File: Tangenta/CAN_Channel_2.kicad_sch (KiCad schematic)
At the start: 18 parts, among them J22 Conn_01x02_Pin, Q3 BSS138, U20 ADM3053

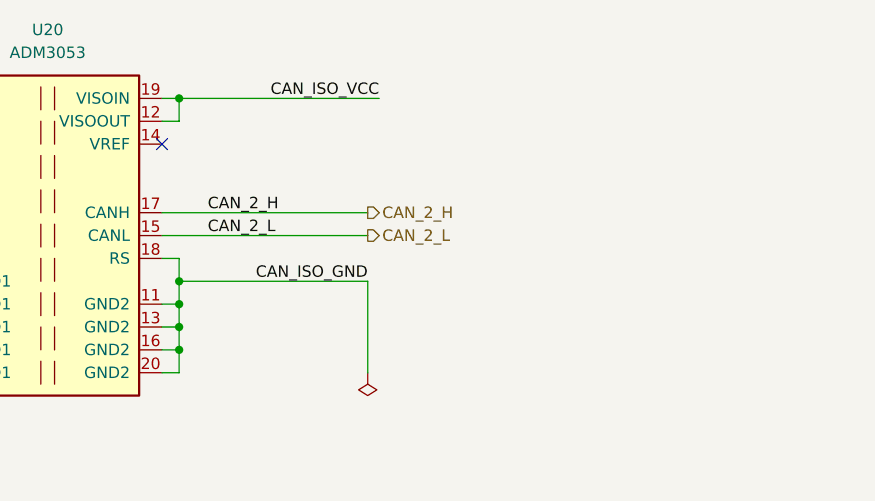
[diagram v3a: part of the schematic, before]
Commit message: CANbus done, UART terminals in progress...
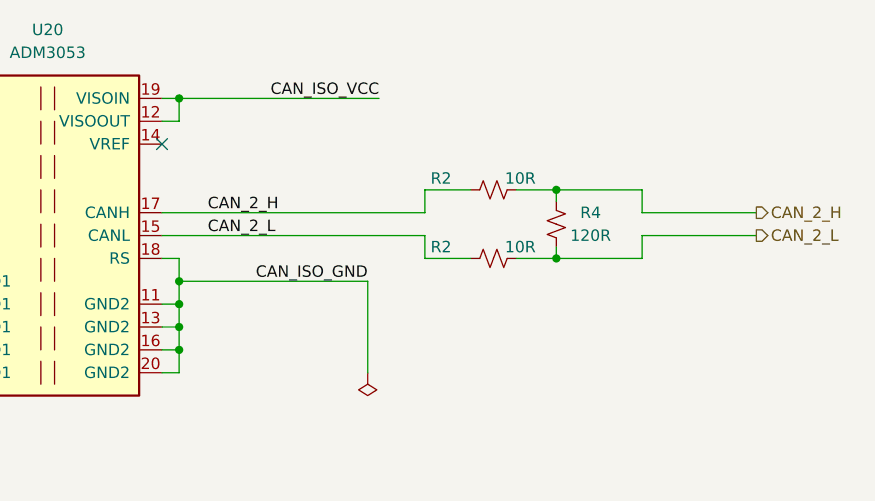
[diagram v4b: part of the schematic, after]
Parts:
- added R2 (x2): 10R, Resistor_SMD:R_0402_1005Metric, symbol Device:R_Small_US
- added R4: 120R, Resistor_SMD:R_0603_1608Metric, symbol Device:R_Small_US
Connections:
- net CAN_2_H: now also R2.1, R2.2, R4.1
- net CAN_2_L: now also R2.1, R2.2, R4.2
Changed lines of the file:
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@@
   (junction (at 124.46 140.97) (diameter 0) (color 0 0 0 0)
   )
+  (junction (at 193.675 77.47) (diameter 0) (color 0 0 0 0)
+  )
   (junction (at 124.46 130.81) (diameter 0) (color 0 0 0 0)
   )
@@
   (junction (at 122.555 85.09) (diameter 0) (color 0 0 0 0)
   )
+  (junction (at 193.675 69.85) (diameter 0) (color 0 0 0 0)
+  )
   (junction (at 80.01 140.97) (diameter 0) (color 0 0 0 0)
   )
@@
   )
   (no_connect (at 149.86 64.77))
+  (wire (pts (xy 193.675 69.85) (xy 193.675 71.12))
+    (stroke (width 0) (type default))
+  )
   (wire (pts (xy 124.46 119.38) (xy 124.46 121.92))
     (stroke (width 0) (type default))
@@
     (stroke (width 0) (type default))
   )
-  (wire (pts (xy 149.86 72.39) (xy 172.72 72.39))
+  (wire (pts (xy 149.86 72.39) (xy 179.07 72.39))
     (stroke (width 0) (type default))
   )
@@
     (stroke (width 0) (type default))
   )
+  (wire (pts (xy 215.9 74.93) (xy 203.2 74.93))
+    (stroke (width 0) (type default))
+  )
   (wire (pts (xy 151.765 90.17) (xy 151.765 87.63))
     (stroke (width 0) (type default))
@@
     (stroke (width 0) (type default))
   )
+  (wire (pts (xy 203.2 69.85) (xy 193.675 69.85))
+    (stroke (width 0) (type default))
+  )
   (wire (pts (xy 151.765 59.69) (xy 173.99 59.69))
     (stroke (width 0) (type default))
@@
     (stroke (width 0) (type default))
   )
+  (wire (pts (xy 189.23 69.85) (xy 193.675 69.85))
+    (stroke (width 0) (type default))
+  )
   (wire (pts (xy 141.605 111.76) (xy 141.605 114.3))
     (stroke (width 0) (type default))
@@
     (stroke (width 0) (type default))
   )
+  (wire (pts (xy 179.07 74.93) (xy 179.07 77.47))
+    (stroke (width 0) (type default))
+  )
   (wire (pts (xy 29.21 140.97) (xy 53.34 140.97))
     (stroke (width 0) (type default))
@@
     (stroke (width 0) (type default))
   )
+  (wire (pts (xy 179.07 72.39) (xy 179.07 69.85))
+    (stroke (width 0) (type default))
+  )
   (wire (pts (xy 122.555 59.69) (xy 113.03 59.69))
     (stroke (width 0) (type default))
   )
+  (wire (pts (xy 189.23 77.47) (xy 193.675 77.47))
+    (stroke (width 0) (type default))
+  )
   (wire (pts (xy 113.03 130.81) (xy 124.46 130.81))
     (stroke (width 0) (type default))
@@
     (stroke (width 0) (type default))
   )
+  (wire (pts (xy 179.07 77.47) (xy 184.15 77.47))
+    (stroke (width 0) (type default))
+  )
   (wire (pts (xy 172.085 140.97) (xy 178.435 140.97))
     (stroke (width 0) (type default))
@@
     (stroke (width 0) (type default))
   )
+  (wire (pts (xy 179.07 69.85) (xy 184.15 69.85))
+    (stroke (width 0) (type default))
+  )
   (wire (pts (xy 53.34 128.27) (xy 53.34 132.08))
     (stroke (width 0) (type default))
@@
     (stroke (width 0) (type default))
   )
-  (wire (pts (xy 149.86 74.93) (xy 172.72 74.93))
+  (wire (pts (xy 149.86 74.93) (xy 179.07 74.93))
     (stroke (width 0) (type default))
   )
@@
     (stroke (width 0) (type default))
   )
+  (wire (pts (xy 193.675 76.2) (xy 193.675 77.47))
+    (stroke (width 0) (type default))
+  )
   (wire (pts (xy 124.46 64.77) (xy 122.555 64.77))
     (stroke (width 0) (type default))
@@
     (stroke (width 0) (type default))
   )
+  (wire (pts (xy 203.2 72.39) (xy 203.2 69.85))
+    (stroke (width 0) (type default))
+  )
   (wire (pts (xy 172.72 90.17) (xy 172.72 80.01))
     (stroke (width 0) (type default))
   )
+  (wire (pts (xy 215.9 72.39) (xy 203.2 72.39))
+    (stroke (width 0) (type default))
+  )
   (wire (pts (xy 151.765 77.47) (xy 149.86 77.47))
     (stroke (width 0) (type default))
@@
   )
   (wire (pts (xy 132.08 119.38) (xy 132.08 121.92))
+    (stroke (width 0) (type default))
+  )
+  (wire (pts (xy 203.2 77.47) (xy 193.675 77.47))
+    (stroke (width 0) (type default))
+  )
+  (wire (pts (xy 203.2 74.93) (xy 203.2 77.47))
     (stroke (width 0) (type default))
   )
@@
     (effects (font (size 1.27 1.27)) (justify right))
   )
-  (hierarchical_label "CAN_2_L" (shape output) (at 172.72 74.93 0) (fields_autoplaced)
+  (hierarchical_label "CAN_2_L" (shape output) (at 215.9 74.93 0) (fields_autoplaced)
     (effects (font (size 1.27 1.27)) (justify left))
   )
-  (hierarchical_label "CAN_2_H" (shape output) (at 172.72 72.39 0) (fields_autoplaced)
+  (hierarchical_label "CAN_2_H" (shape output) (at 215.9 72.39 0) (fields_autoplaced)
     (effects (font (size 1.27 1.27)) (justify left))
   )
@@
     )
   )
+  (symbol (lib_id "Device:R_Small_US") (at 193.675 73.66 0) (unit 1)
+    (in_bom yes) (on_board yes) (dnp no)
+    (property "Reference" "R4" (at 197.485 72.39 0)
+      (effects (font (size 1.27 1.27)))
+    )
+    (property "Value" "120R" (at 197.485 74.93 0)
+      (effects (font (size 1.27 1.27)))
+    )
+    (property "Footprint" "Resistor_SMD:R_0603_1608Metric" (at 193.675 73.66 0)
+      (effects (font (size 1.27 1.27)) hide)
+    )
+    (property "Datasheet" "~" (at 193.675 73.66 0)
+      (effects (font (size 1.27 1.27)) hide)
+    )
+    (pin "1")
+    (pin "2")
+    (instances
+      (project "Tangenta"
+        (path "/358d1bcf-7599-4352-8c4d-baa18a5f09e6/8215796b-9611-4f43-bcc5-319f8414b8a6"
+          (reference "R4") (unit 1)
+        )
+        (path "/358d1bcf-7599-4352-8c4d-baa18a5f09e6/98e3b24f-9927-4339-b8fd-9deea91a522a"
+          (reference "R182") (unit 1)
+        )
+        (path "/358d1bcf-7599-4352-8c4d-baa18a5f09e6/b5394a48-5ef8-44c9-9d56-604d4ce6d7c8/96e01dc6-7803-4642-812e-1845a7add5da"
+          (reference "R184") (unit 1)
+        )
+        (path "/358d1bcf-7599-4352-8c4d-baa18a5f09e6/b5394a48-5ef8-44c9-9d56-604d4ce6d7c8/9d7e074a-447f-4471-b1b0-91eb27649d54"
+          (reference "R187") (unit 1)
+        )
+      )
+    )
+  )
   (symbol (lib_id "power:GNDREF") (at 113.03 140.97 0) (unit 1)
     (in_bom yes) (on_board yes) (dnp no) (fields_autoplaced)
@@
         )
       )
+    )
+  )
+  (symbol (lib_id "Device:R_Small_US") (at 186.69 77.47 270) (unit 1)
+    (in_bom yes) (on_board yes) (dnp no)
+    (property "Reference" "R2" (at 179.705 76.2 90)
+      (effects (font (size 1.27 1.27)) (justify left))
+    )
+    (property "Value" "10R" (at 187.96 76.2 90)
+      (effects (font (size 1.27 1.27)) (justify left))
+    )
+    (property "Footprint" "Resistor_SMD:R_0402_1005Metric" (at 186.69 77.47 0)
+      (effects (font (size 1.27 1.27)) hide)
+    )
+    (property "Datasheet" "~" (at 186.69 77.47 0)
+      (effects (font (size 1.27 1.27)) hide)
+    )
+    (pin "1")
+    (pin "2")
+    (instances
+      (project "Tangenta"
+        (path "/358d1bcf-7599-4352-8c4d-baa18a5f09e6/8215796b-9611-4f43-bcc5-319f8414b8a6"
+          (reference "R2") (unit 1)
+        )
+        (path "/358d1bcf-7599-4352-8c4d-baa18a5f09e6/d6c05402-162e-441f-bed8-be7996260fb4"
+          (reference "R18") (unit 1)
+        )
+        (path "/358d1bcf-7599-4352-8c4d-baa18a5f09e6/b1871a4d-6a35-44e2-a9a2-9a4af684371d"
+          (reference "R26") (unit 1)
+        )
+        (path "/358d1bcf-7599-4352-8c4d-baa18a5f09e6/6a8c68b5-4a7d-449e-86f6-34ced6d1cb55"
+          (reference "R41") (unit 1)
+        )
+        (path "/358d1bcf-7599-4352-8c4d-baa18a5f09e6/db297b0b-35f2-4e86-892c-83973f1ac2db"
+          (reference "R41") (unit 1)
+        )
+        (path "/358d1bcf-7599-4352-8c4d-baa18a5f09e6/98e3b24f-9927-4339-b8fd-9deea91a522a"
+          (reference "R153") (unit 1)
+        )
+        (path "/358d1bcf-7599-4352-8c4d-baa18a5f09e6/b5394a48-5ef8-44c9-9d56-604d4ce6d7c8/96e01dc6-7803-4642-812e-1845a7add5da"
+          (reference "R168") (unit 1)
+        )
+        (path "/358d1bcf-7599-4352-8c4d-baa18a5f09e6/b5394a48-5ef8-44c9-9d56-604d4ce6d7c8/9d7e074a-447f-4471-b1b0-91eb27649d54"
+          (reference "R186") (unit 1)
+        )
+      )
+    )
+  )
+  (symbol (lib_id "Device:R_Small_US") (at 186.69 69.85 270) (unit 1)
+    (in_bom yes) (on_board yes) (dnp no)
+    (property "Reference" "R2" (at 179.705 68.58 90)
+      (effects (font (size 1.27 1.27)) (justify left))
+    )
+    (property "Value" "10R" (at 187.96 68.58 90)
+      (effects (font (size 1.27 1.27)) (justify left))
+    )
+    (property "Footprint" "Resistor_SMD:R_0402_1005Metric" (at 186.69 69.85 0)
+      (effects (font (size 1.27 1.27)) hide)
+    )
+    (property "Datasheet" "~" (at 186.69 69.85 0)
+      (effects (font (size 1.27 1.27)) hide)
+    )
+    (pin "1")
+    (pin "2")
+    (instances
+      (project "Tangenta"
+        (path "/358d1bcf-7599-4352-8c4d-baa18a5f09e6/8215796b-9611-4f43-bcc5-319f8414b8a6"
+          (reference "R2") (unit 1)
+        )
+        (path "/358d1bcf-7599-4352-8c4d-baa18a5f09e6/d6c05402-162e-441f-bed8-be7996260fb4"
+          (reference "R18") (unit 1)
+        )
+        (path "/358d1bcf-7599-4352-8c4d-baa18a5f09e6/b1871a4d-6a35-44e2-a9a2-9a4af684371d"
+          (reference "R26") (unit 1)
+        )
+        (path "/358d1bcf-7599-4352-8c4d-baa18a5f09e6/6a8c68b5-4a7d-449e-86f6-34ced6d1cb55"
+          (reference "R41") (unit 1)
+        )
+        (path "/358d1bcf-7599-4352-8c4d-baa18a5f09e6/db297b0b-35f2-4e86-892c-83973f1ac2db"
+          (reference "R41") (unit 1)
+        )
+        (path "/358d1bcf-7599-4352-8c4d-baa18a5f09e6/98e3b24f-9927-4339-b8fd-9deea91a522a"
+          (reference "R152") (unit 1)
+        )
+        (path "/358d1bcf-7599-4352-8c4d-baa18a5f09e6/b5394a48-5ef8-44c9-9d56-604d4ce6d7c8/96e01dc6-7803-4642-812e-1845a7add5da"
+          (reference "R151") (unit 1)
+        )
+        (path "/358d1bcf-7599-4352-8c4d-baa18a5f09e6/b5394a48-5ef8-44c9-9d56-604d4ce6d7c8/9d7e074a-447f-4471-b1b0-91eb27649d54"
+          (reference "R185") (unit 1)
+        )
+      )

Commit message: Libraries exported from global to project.
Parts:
- C1: symbol Device:C_Small -> CholaSymbolsPrjLib:C_Small
- FB1: symbol Ferrite_Bead_100:GZ2012D101TF -> CholaSymbolsPrjLib:GZ2012D101TF
- J22: symbol Connector:Conn_01x02_Pin -> CholaSymbolsPrjLib:Conn_01x02_Pin
- Q3: symbol Transistor_FET:BSS138 -> CholaSymbolsPrjLib:BSS138
- R2, R4: symbol Device:R_Small_US -> CholaSymbolsPrjLib:R_Small_US
- U20: symbol Interface_CAN_LIN:ADM3053 -> CholaSymbolsPrjLib:ADM3053
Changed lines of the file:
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@@
     (effects (font (size 1.27 1.27)) (justify left))
   )
-  (symbol (lib_id "Device:R_Small_US") (at 80.01 134.62 180) (unit 1)
+  (symbol (lib_id "CholaSymbolsPrjLib:R_Small_US") (at 80.01 134.62 180) (unit 1)
     (in_bom yes) (on_board yes) (dnp no)
     (property "Reference" "R2" (at 78.74 133.35 0)
@@
     )
   )
-  (symbol (lib_id "Transistor_FET:BSS138") (at 66.04 138.43 270) (unit 1)
+  (symbol (lib_id "CholaSymbolsPrjLib:BSS138") (at 66.04 138.43 270) (unit 1)
     (in_bom yes) (on_board yes) (dnp no)
     (property "Reference" "Q3" (at 68.58 135.89 90)
@@
     )
   )
-  (symbol (lib_id "Device:C_Small") (at 132.08 135.89 180) (unit 1)
+  (symbol (lib_id "CholaSymbolsPrjLib:C_Small") (at 132.08 135.89 180) (unit 1)
     (in_bom yes) (on_board yes) (dnp no)
     (property "Reference" "C1" (at 129.5399 133.9849 0)
@@
     )
   )
-  (symbol (lib_id "Device:C_Small") (at 124.46 116.84 180) (unit 1)
+  (symbol (lib_id "CholaSymbolsPrjLib:C_Small") (at 124.46 116.84 180) (unit 1)
     (in_bom yes) (on_board yes) (dnp no)
     (property "Reference" "C1" (at 121.9199 114.9349 0)
@@
     )
   )
-  (symbol (lib_id "Device:R_Small_US") (at 53.34 134.62 180) (unit 1)
+  (symbol (lib_id "CholaSymbolsPrjLib:R_Small_US") (at 53.34 134.62 180) (unit 1)
     (in_bom yes) (on_board yes) (dnp no)
     (property "Reference" "R2" (at 52.07 133.35 0)
@@
     )
   )
-  (symbol (lib_id "Transistor_FET:BSS138") (at 66.04 117.475 270) (unit 1)
+  (symbol (lib_id "CholaSymbolsPrjLib:BSS138") (at 66.04 117.475 270) (unit 1)
     (in_bom yes) (on_board yes) (dnp no)
     (property "Reference" "Q3" (at 68.58 114.935 90)
@@
     )
   )
-  (symbol (lib_id "Connector:Conn_01x02_Pin") (at 139.065 153.67 270) (unit 1)
+  (symbol (lib_id "CholaSymbolsPrjLib:Conn_01x02_Pin") (at 139.065 153.67 270) (unit 1)
     (in_bom yes) (on_board yes) (dnp no)
     (property "Reference" "J22" (at 135.89 152.4 90)
@@
     )
   )
-  (symbol (lib_id "Device:C_Small") (at 159.385 135.89 0) (mirror x) (unit 1)
+  (symbol (lib_id "CholaSymbolsPrjLib:C_Small") (at 159.385 135.89 0) (mirror x) (unit 1)
     (in_bom yes) (on_board yes) (dnp no)
     (property "Reference" "C1" (at 161.9251 133.9849 0)
@@
     )
   )
-  (symbol (lib_id "Device:R_Small_US") (at 80.01 113.665 180) (unit 1)
+  (symbol (lib_id "CholaSymbolsPrjLib:R_Small_US") (at 80.01 113.665 180) (unit 1)
     (in_bom yes) (on_board yes) (dnp no)
     (property "Reference" "R2" (at 78.74 112.395 0)
@@
     )
   )
-  (symbol (lib_id "Device:C_Small") (at 124.46 135.89 180) (unit 1)
+  (symbol (lib_id "CholaSymbolsPrjLib:C_Small") (at 124.46 135.89 180) (unit 1)
     (in_bom yes) (on_board yes) (dnp no)
     (property "Reference" "C1" (at 121.9199 133.9849 0)
@@
     )
   )
-  (symbol (lib_id "Device:C_Small") (at 132.08 116.84 180) (unit 1)
+  (symbol (lib_id "CholaSymbolsPrjLib:C_Small") (at 132.08 116.84 180) (unit 1)
     (in_bom yes) (on_board yes) (dnp no)
     (property "Reference" "C1" (at 129.5399 114.9349 0)
@@
     )
   )
-  (symbol (lib_id "Device:C_Small") (at 141.605 116.84 0) (mirror x) (unit 1)
+  (symbol (lib_id "CholaSymbolsPrjLib:C_Small") (at 141.605 116.84 0) (mirror x) (unit 1)
     (in_bom yes) (on_board yes) (dnp no)
     (property "Reference" "C1" (at 144.1451 114.9349 0)
@@
     )
   )
-  (symbol (lib_id "Device:R_Small_US") (at 193.675 73.66 0) (unit 1)
+  (symbol (lib_id "CholaSymbolsPrjLib:R_Small_US") (at 193.675 73.66 0) (unit 1)
     (in_bom yes) (on_board yes) (dnp no)
     (property "Reference" "R4" (at 197.485 72.39 0)
@@
     )
   )
-  (symbol (lib_id "Ferrite_Bead_100:GZ2012D101TF") (at 168.91 130.81 0) (unit 1)
+  (symbol (lib_id "CholaSymbolsPrjLib:GZ2012D101TF") (at 168.91 130.81 0) (unit 1)
     (in_bom yes) (on_board yes) (dnp no)
     (property "Reference" "FB1" (at 168.91 128.27 0)
@@
     )
   )
-  (symbol (lib_id "Device:C_Small") (at 160.655 116.84 0) (mirror x) (unit 1)
+  (symbol (lib_id "CholaSymbolsPrjLib:C_Small") (at 160.655 116.84 0) (mirror x) (unit 1)
     (in_bom yes) (on_board yes) (dnp no)
     (property "Reference" "C1" (at 163.1951 114.9349 0)
@@
     )
   )
-  (symbol (lib_id "Device:R_Small_US") (at 53.34 113.665 180) (unit 1)
+  (symbol (lib_id "CholaSymbolsPrjLib:R_Small_US") (at 53.34 113.665 180) (unit 1)
     (in_bom yes) (on_board yes) (dnp no)
     (property "Reference" "R2" (at 52.07 112.395 0)
@@
     )
   )
-  (symbol (lib_id "Device:R_Small_US") (at 186.69 77.47 270) (unit 1)
+  (symbol (lib_id "CholaSymbolsPrjLib:R_Small_US") (at 186.69 77.47 270) (unit 1)
     (in_bom yes) (on_board yes) (dnp no)
     (property "Reference" "R2" (at 179.705 76.2 90)
@@
     )
   )
-  (symbol (lib_id "Device:R_Small_US") (at 186.69 69.85 270) (unit 1)
+  (symbol (lib_id "CholaSymbolsPrjLib:R_Small_US") (at 186.69 69.85 270) (unit 1)
     (in_bom yes) (on_board yes) (dnp no)
     (property "Reference" "R2" (at 179.705 68.58 90)
@@
     )
   )
-  (symbol (lib_id "Interface_CAN_LIN:ADM3053") (at 137.16 74.93 0) (unit 1)
+  (symbol (lib_id "CholaSymbolsPrjLib:ADM3053") (at 137.16 74.93 0) (unit 1)
     (in_bom yes) (on_board yes) (dnp no) (fields_autoplaced)
     (property "Reference" "U20" (at 137.16 52.07 0)
@@
     )
   )
-  (symbol (lib_id "Ferrite_Bead_100:GZ2012D101TF") (at 168.91 140.97 0) (unit 1)
+  (symbol (lib_id "CholaSymbolsPrjLib:GZ2012D101TF") (at 168.91 140.97 0) (unit 1)
     (in_bom yes) (on_board yes) (dnp no)
     (property "Reference" "FB1" (at 168.91 138.43 0)
@@
     )
   )
-  (symbol (lib_id "Device:C_Small") (at 178.435 135.89 0) (mirror x) (unit 1)
+  (symbol (lib_id "CholaSymbolsPrjLib:C_Small") (at 178.435 135.89 0) (mirror x) (unit 1)
     (in_bom yes) (on_board yes) (dnp no)
     (property "Reference" "C1" (at 180.9751 133.9849 0)

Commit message: GND ready, before re-annotation.
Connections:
- net CAN_2_H: no longer R2.2, U20.17 (CANH)
- net CAN_2_L: no longer R2.2, U20.15 (CANL)
- new net CAN_2_H_IC: R2.2, U20.17 (CANH)
- new net CAN_2_L_IC: R2.2, U20.15 (CANL)
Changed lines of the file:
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@@
     (stroke (width 0) (type default))
   )
-  (label "CAN_2_L" (at 154.94 74.93 0) (fields_autoplaced)
+  (label "CAN_2_L_IC" (at 154.94 74.93 0) (fields_autoplaced)
     (effects (font (size 1.27 1.27)) (justify left bottom))
   )
@@
     (effects (font (size 1.27 1.27)) (justify left bottom))
   )
-  (label "CAN_2_H" (at 154.94 72.39 0) (fields_autoplaced)
+  (label "CAN_2_H_IC" (at 154.94 72.39 0) (fields_autoplaced)
     (effects (font (size 1.27 1.27)) (justify left bottom))
   )
